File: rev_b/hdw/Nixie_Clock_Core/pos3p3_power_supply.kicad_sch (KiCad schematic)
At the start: 27 parts, among them Q401 BSS214NW, Q402 ZXMS6004FFTA, U401 74LVC1G97, U402 TPS62132

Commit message: lots of rev B control board schematic progress
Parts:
- removed C401, C405: 0.1uF, Capacitors_SMD:C_0402, symbol Custom_Library:C_Custom
- removed C402, C406, C407: 10uF, Capacitors_SMD:C_1206, symbol Custom_Library:C_Custom
- removed C404: 10nF, Capacitors_SMD:C_0402, symbol Custom_Library:C_Custom
- removed L401: 2.2uH, Inductors_SMD:L_Vishay_IHLP-2020, symbol Custom_Library:L_Custom
- removed R401, R403: 10k, Resistors_SMD:R_0402, symbol Custom_Library:R_Custom
- removed R405: 0, Resistors_SMD:R_0402, symbol Custom_Library:R_Custom
- removed R412: 562k, Resistors_SMD:R_0402, symbol Custom_Library:R_Custom
- removed R413: 180k, Resistors_SMD:R_0402, symbol Custom_Library:R_Custom
- removed U401: 74LVC1G97, Package_TO_SOT_SMD:SOT-363_SC-70-6, symbol Custom_Library:74LVC1G97_Power_AND
- removed U402: TPS62132, Package_DFN_QFN:QFN-16-1EP_3x3mm_P0.5mm_EP1.8x1.8mm, symbol Custom_Library:TPS62130
- added C? (x4): 10uF, symbol Custom Library:C_Custom
- added C?: 10nF, Capacitors_SMD:C_0402, symbol Custom_Library:C_Custom
- added C?: 4.7uF, Capacitors_SMD:C_0805, symbol Custom_Library:C_Custom
- added C?: 47pF, Capacitors_SMD:C_0603, symbol Custom_Library:C_Custom
- added C?: 0.1uF, Capacitors_SMD:C_0603, symbol Custom_Library:C_Custom
- added L?: 2.2uH, Inductor_SMD:L_Vishay_IHLP-2020, symbol Custom Library:L_Custom
- added R?: 1M, Resistors_SMD:R_0402, symbol Custom_Library:R_Custom
- added R?: 18.2k, Resistors_SMD:R_0402, symbol Custom_Library:R_Custom
- added R?: 10k, Resistors_SMD:R_0402, symbol Custom_Library:R_Custom
- added R?: 309k, Resistors_SMD:R_0402, symbol Custom_Library:R_Custom
- added U?: LT8609A-DD, Housings_DFN_QFN:DFN-10-1EP_3x3mm_Pitch0.5mm, symbol Custom Library:LT8609A-DD
- renumbered C403 to C?, D401 to D?, Q401 to Q?, Q402 to Q?, R404 to R?, R409 to R?, R406 to R?, R407 to R?, R410 to R?, R402 to R?, R408 to R?, R411 to R?, TP401 to TP?
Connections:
- net +3.3V: now also C?.1, R?.1, R?.1
- net GND: now also C?.2, C?.2, C?.2, C?.2, C?.2, C?.2, R?.2, R?.2, U?.11 (GND)
- net POS3P3_PGOOD: now also R?.2, U?.8 (PG)
- net POS3P3_RUN: now also U?.10 (EN/UV)
- net at R?.1, R?.1, R?.1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: now also C?.1, C?.1, L?.2
- net POS12_PGOOD renamed POS24_PGOOD
- new net: C?.2, L?.1, U?.2 (SW)
- new net: C?.2, R?.1, R?.2, U?.6 (FB)
- new net: C?.1, U?.7 (TR/SS)
- new net: R?.1, U?.4 (RT)
- new net: C?.1, U?.3 (INTVCC), U?.5 (SYNC)
- new net: C?.1, U?.1 (BST)
- new net +24V: C?.1, C?.1, U?.9 (VIN)
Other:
- note removed: "Fixed VOUT = +3.3V"
- moved on the sheet: C?, D?, Q?, R?, TP?

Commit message: more rev b sch progress
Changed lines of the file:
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@@
     (stroke (width 0) (type default))
   )
-  (wire (pts (xy 146.05 80.01) (xy 129.54 80.01))
+  (wire (pts (xy 137.16 80.01) (xy 129.54 80.01))
     (stroke (width 0) (type default))
   )
@@
     (stroke (width 0) (type default))
   )
-  (wire (pts (xy 146.05 97.79) (xy 146.05 80.01))
+  (wire (pts (xy 137.16 97.79) (xy 137.16 80.01))
     (stroke (width 0) (type default))
   )
@@
     (stroke (width 0) (type default))
   )
-  (wire (pts (xy 146.05 97.79) (xy 213.36 97.79))
+  (wire (pts (xy 137.16 97.79) (xy 213.36 97.79))
     (stroke (width 0) (type default))
   )

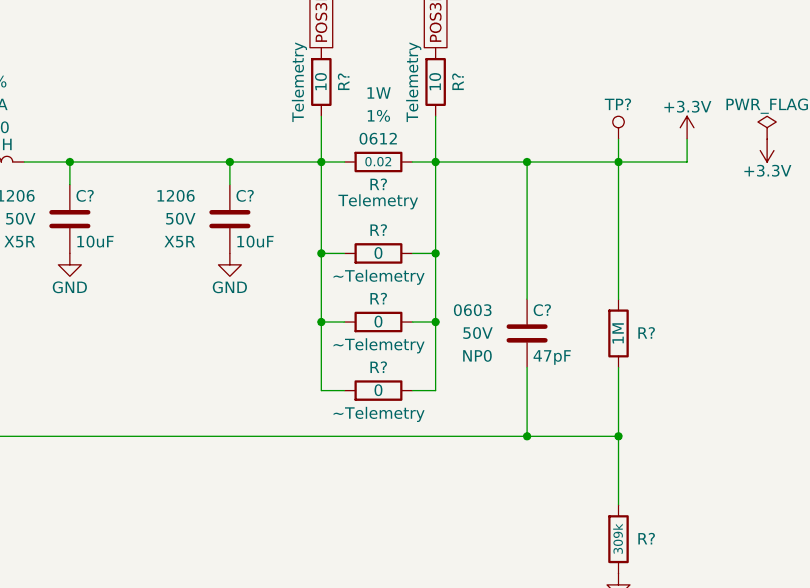
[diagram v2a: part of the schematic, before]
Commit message: revamped POS180 telemetry
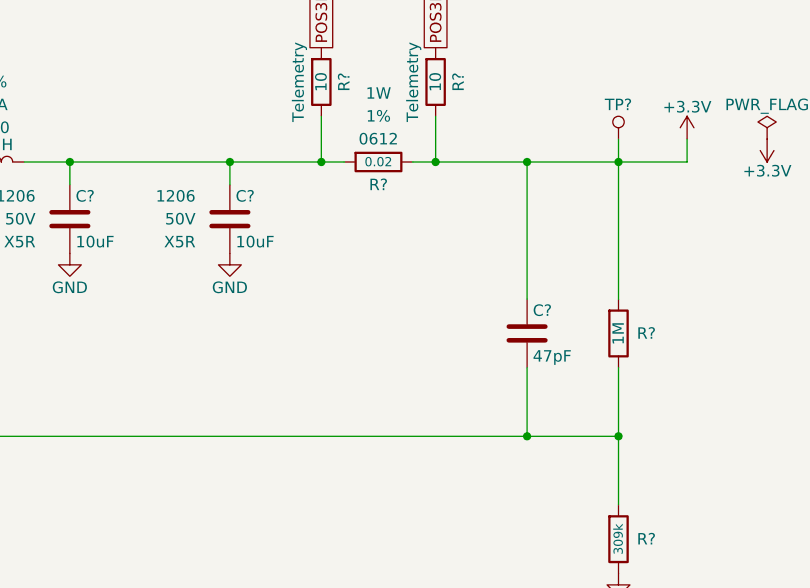
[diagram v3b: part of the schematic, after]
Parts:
- removed R? (x3): 0, Resistors_SMD:R_0402, symbol Custom_Library:R_Custom
- R?: Configuration Telemetry -> (none)

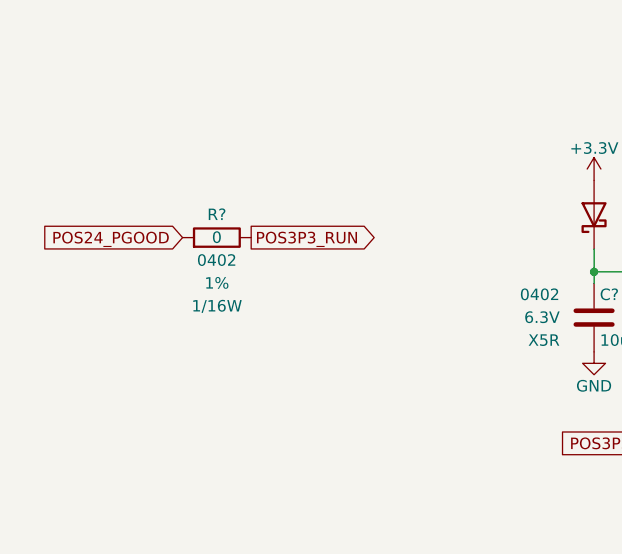
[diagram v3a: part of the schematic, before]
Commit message: more schematic progress, assigning signals to MCU"
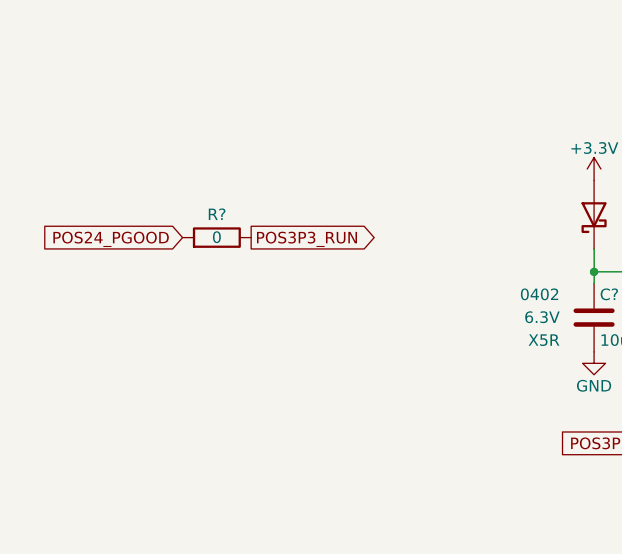
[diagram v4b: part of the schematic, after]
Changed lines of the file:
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@@
     )
     (property "display_footprint" "0402" (at 46.99 168.91 90)
-      (effects (font (size 1.27 1.27)))
+      (effects (font (size 1.27 1.27)) hide)
     )
     (property "Tolerance" "1%" (at 46.99 171.45 90)
-      (effects (font (size 1.27 1.27)))
+      (effects (font (size 1.27 1.27)) hide)
     )
     (property "Wattage" "1/16W" (at 46.99 173.99 90)
-      (effects (font (size 1.27 1.27)))
+      (effects (font (size 1.27 1.27)) hide)
     )
     (property "Digi-Key PN" "RMCF0402ZT0R00CT-ND" (at 46.99 166.37 0)

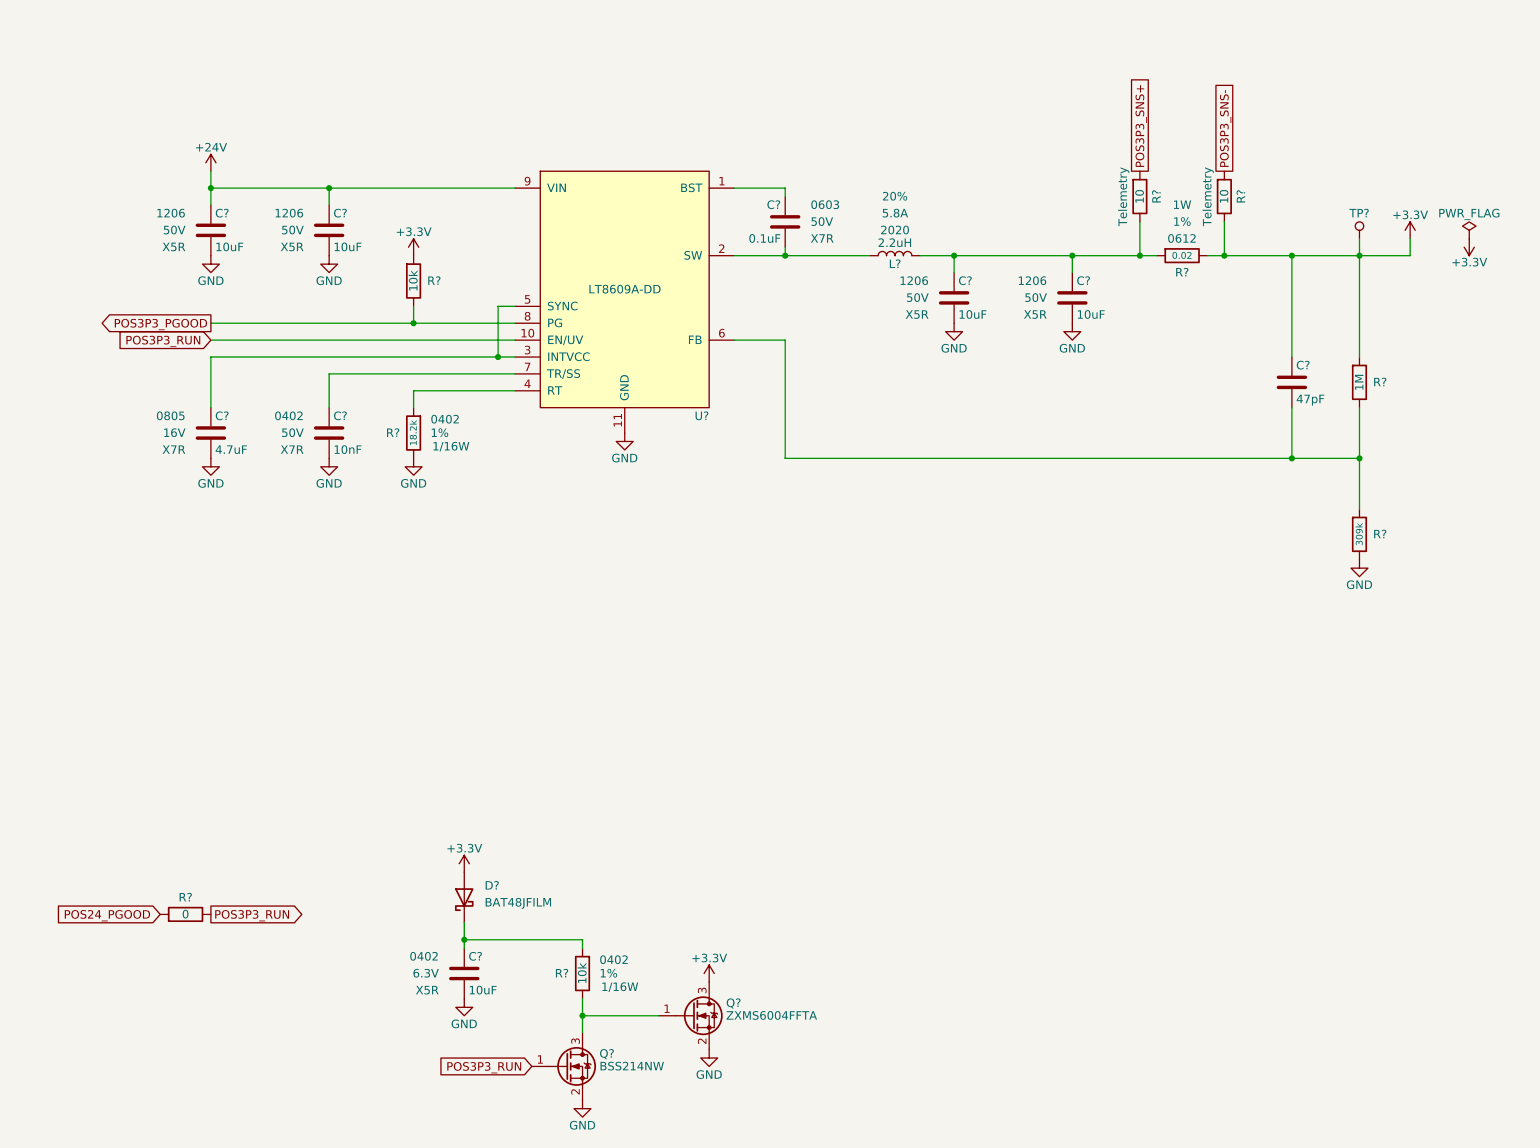
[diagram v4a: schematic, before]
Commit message: updated footprints, ran some DRC
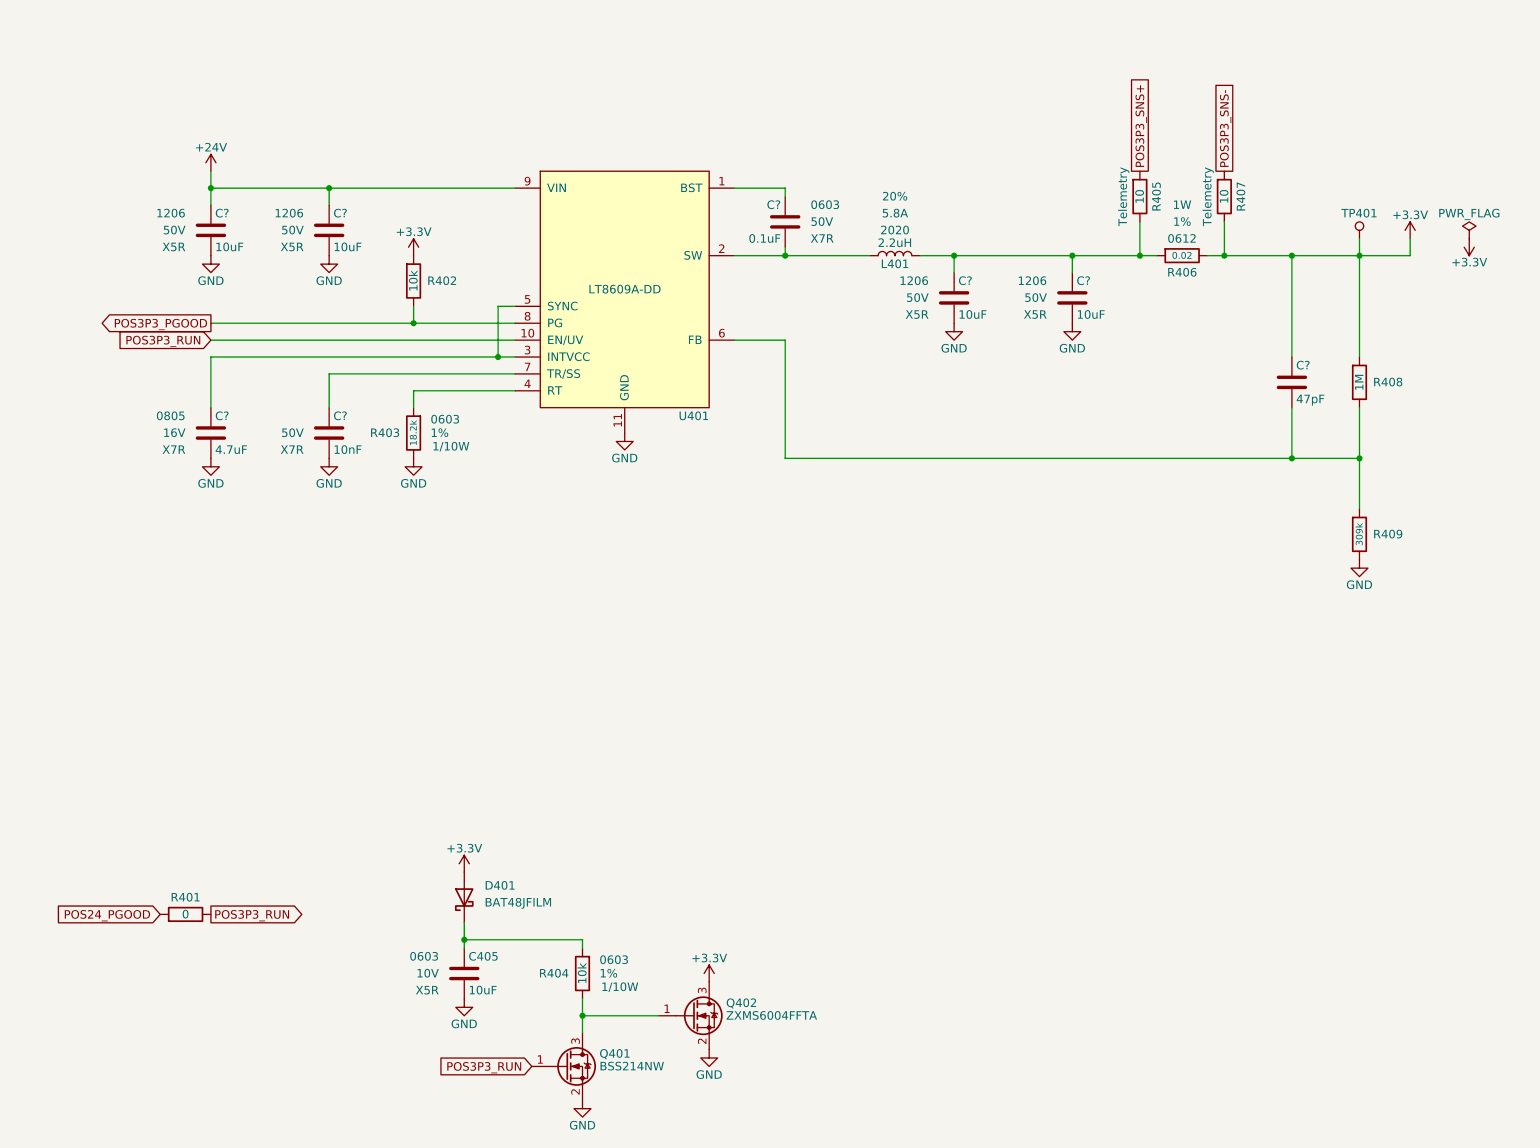
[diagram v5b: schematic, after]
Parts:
- C405: renamed from C?; footprint Capacitors_SMD:C_0402 -> Capacitors_SMD:C_0603; Digi-Key PN 1276-1451-1-ND -> (none); Voltage 6.3V -> 10V; display_footprint 0402 -> 0603
- C? (x4): footprint (none) -> Capacitors_SMD:C_1206; Digi-Key PN 1276-6736-1-ND -> (none)
- C?: footprint Capacitors_SMD:C_0402 -> Capacitors_SMD:C_0603; Digi-Key PN 399-3066-1-ND -> (none); display_footprint 0402 -> (none)
- C?: Digi-Key PN 1276-2970-1-ND -> (none)
- C?: Digi-Key PN 399-7918-1-ND -> (none)
- C?: Digi-Key PN 399-7845-1-ND -> (none)
- R401: renamed from R?; footprint Resistors_SMD:R_0402 -> Resistors_SMD:R_0603; Digi-Key PN RMCF0402ZT0R00CT-ND -> (none); Wattage 1/16W -> 1/10W; display_footprint 0402 -> 0603
- R402, R404: renamed from R?; footprint Resistors_SMD:R_0402 -> Resistors_SMD:R_0603; Digi-Key PN RMCF0402FT10K0CT-ND -> (none); Wattage 1/16W -> 1/10W; display_footprint 0402 -> 0603
- R403, R408, R409: renamed from R?; footprint Resistors_SMD:R_0402 -> Resistors_SMD:R_0603; Wattage 1/16W -> 1/10W; display_footprint 0402 -> 0603
- R405, R407: renamed from R?; footprint Resistors_SMD:R_0402 -> Resistors_SMD:R_0603; Digi-Key PN RMCF0402FT10R0CT-ND -> (none); Wattage 1/16W -> 1/10W; display_footprint 0402 -> 0603
- gave numbers to parts that had none: 7

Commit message: hid all passive refdes on core PCB
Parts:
- C405: Digi-Key PN (none) -> 1276-1871-1-ND
- C? (x4): Digi-Key PN (none) -> 1276-6767-1-ND
- C?: Digi-Key PN (none) -> 1276-1009-1-ND; display_footprint (none) -> 0603
- C?: Digi-Key PN (none) -> 1276-2970-1-ND
- C?: Digi-Key PN (none) -> 13-CC0603JPNPO9BN470CT-ND
- C?: Digi-Key PN (none) -> 1276-1935-1-ND
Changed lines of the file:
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@@
       (effects (font (size 1.27 1.27)) (justify right))
     )
-    (property "Digi-Key PN" "" (at 88.9 175.26 0)
+    (property "Digi-Key PN" "1276-1871-1-ND" (at 88.9 175.26 0)
       (effects (font (size 1.27 1.27)) hide)
     )
@@
       (effects (font (size 1.27 1.27)) (justify right))
     )
-    (property "Digi-Key PN" "" (at 173.355 60.96 0)
+    (property "Digi-Key PN" "1276-6767-1-ND" (at 173.355 60.96 0)
       (effects (font (size 1.524 1.524)) hide)
     )
@@
       (effects (font (size 1.27 1.27)) hide)
     )
-    (property "display_footprint" "" (at 64.77 91.44 0)
+    (property "display_footprint" "0603" (at 64.77 91.44 0)
       (effects (font (size 1.27 1.27)) (justify right))
     )
@@
       (effects (font (size 1.27 1.27)) (justify right))
     )
-    (property "Digi-Key PN" "" (at 79.375 81.28 0)
+    (property "Digi-Key PN" "1276-1009-1-ND" (at 79.375 81.28 0)
       (effects (font (size 1.524 1.524)) hide)
     )
@@
       (effects (font (size 1.27 1.27)) (justify right))
     )
-    (property "Digi-Key PN" "" (at -99.06 209.804 0)
+    (property "Digi-Key PN" "1276-2970-1-ND" (at -99.06 209.804 0)
       (effects (font (size 1.27 1.27)) hide)
     )
@@
       (effects (font (size 1.27 1.27)) (justify right) hide)
     )
-    (property "Digi-Key PN" "" (at 213.36 86.36 0)
+    (property "Digi-Key PN" "13-CC0603JPNPO9BN470CT-ND" (at 213.36 86.36 0)
       (effects (font (size 1.27 1.27)) hide)
     )
@@
       (effects (font (size 1.27 1.27)) hide)
     )
-    (property "Digi-Key PN" "" (at 126.365 49.53 0)
+    (property "Digi-Key PN" "1276-1935-1-ND" (at 126.365 49.53 0)
       (effects (font (size 1.524 1.524)) hide)
     )
@@
       (effects (font (size 1.27 1.27)) (justify right))
     )
-    (property "Digi-Key PN" "" (at 79.375 50.8 0)
+    (property "Digi-Key PN" "1276-6767-1-ND" (at 79.375 50.8 0)
       (effects (font (size 1.524 1.524)) hide)
     )
@@
       (effects (font (size 1.27 1.27)) (justify right))
     )
-    (property "Digi-Key PN" "" (at 61.595 50.8 0)
+    (property "Digi-Key PN" "1276-6767-1-ND" (at 61.595 50.8 0)
       (effects (font (size 1.524 1.524)) hide)
     )
@@
       (effects (font (size 1.27 1.27)) (justify right))
     )
-    (property "Digi-Key PN" "" (at 191.135 60.96 0)
+    (property "Digi-Key PN" "1276-6767-1-ND" (at 191.135 60.96 0)
       (effects (font (size 1.524 1.524)) hide)
     )
